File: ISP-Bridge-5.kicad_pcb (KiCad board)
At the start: 2 copper layers, 15.2 x 35.6 mm, 7 parts, among them IC1 ATMEGA328-P, J1 ATMEL_ISP_6PIN, SW1 SW_PUSH

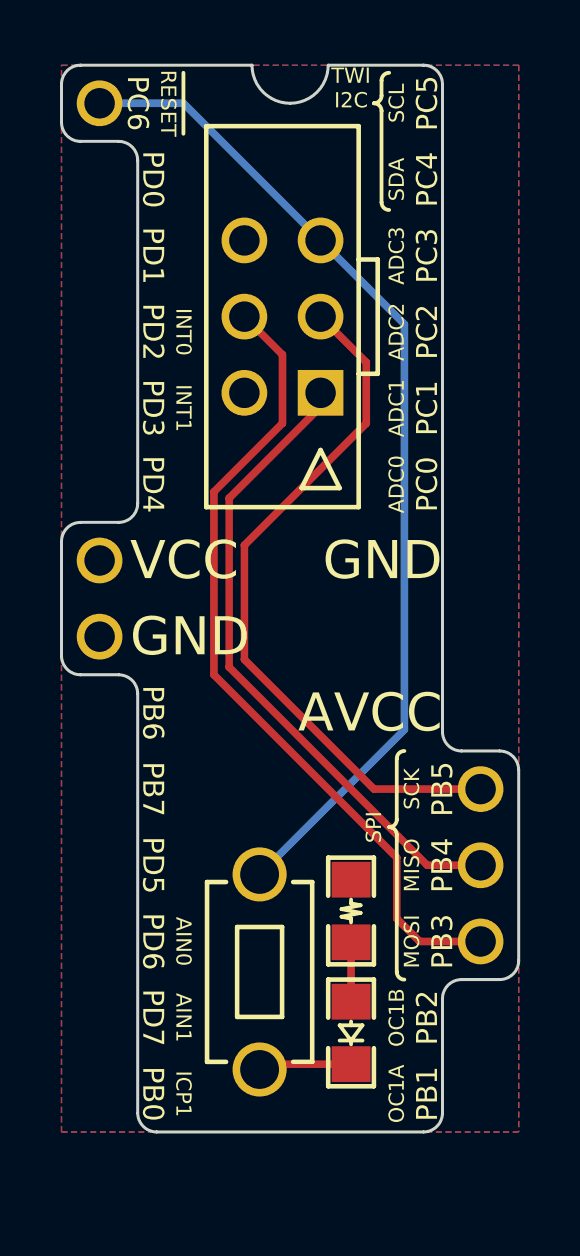
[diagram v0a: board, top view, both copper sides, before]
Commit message: Updated for KiCad 4.0.2, uses pretty libraries
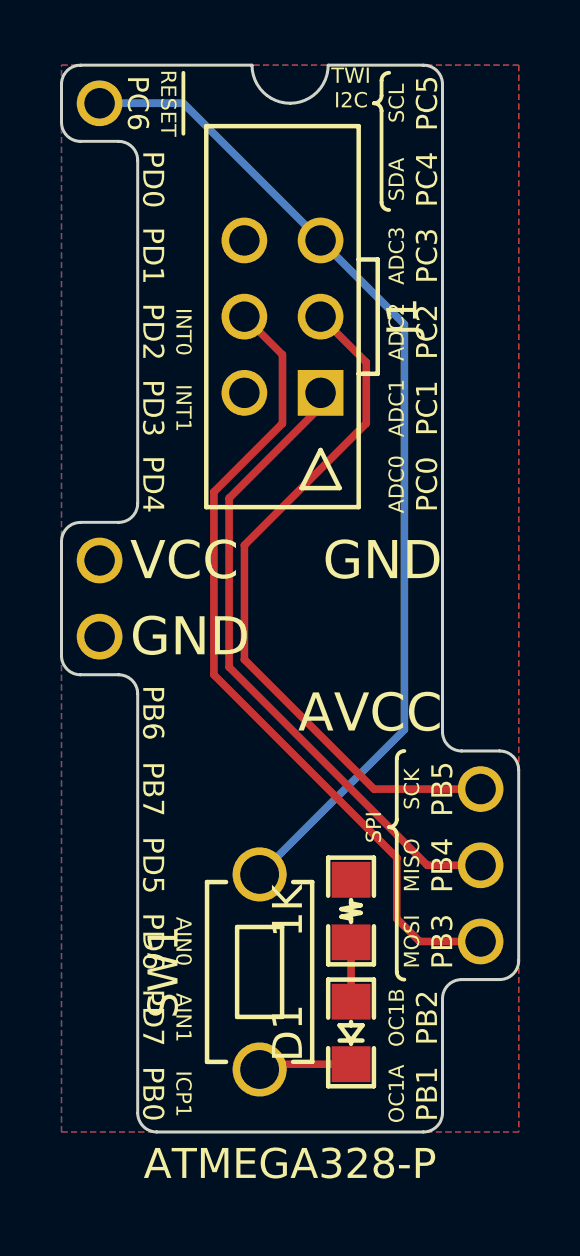
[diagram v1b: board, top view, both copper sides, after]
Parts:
- D1: footprint LED0805-sym -> Ossicone_Labs_Footprints:LED_0805_Symbol
- IC1: footprint ATmegax8 -> Ossicone_Labs_Footprints:Atmel_ATtiny-x8_ATmega-x8
- J1: footprint ATMEL_ISP_6PIN -> Ossicone_Labs_Footprints:Atmel_ISP_6PIN
- R1: footprint R0805-sym -> Ossicone_Labs_Footprints:R_0805_Symbol
- SW1: footprint MJTP1250 -> Ossicone_Labs_Footprints:SW_PUSH_MJTP1250
- turned D1 to 90 degrees
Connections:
- D1 pad 1: N-000004 -> GND
- D1 pad 2: GND -> Net-(D1-Pad2)
- R1 pad 1: N-000004 -> Net-(D1-Pad2)
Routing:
- net Net-(D1-Pad2): track 0.00 -> 1.98 mm
- net N-000004: track 1.98 -> 0.00 mm

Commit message: Rev 1.1 - changed rev number on board and 16 -> 32 segment on floodfills
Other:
- board text added: "v1.1"
- board text removed: "v1.0"
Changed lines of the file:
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@@
     (links 11)
     (no_connects 0)
-    (area 195.529999 107.899999 210.870001 143.560001)
+    (area 195.529999 105.701254 210.870001 145.608746)
     (thickness 1.6)
     (drawings 106)
@@
   (layers
     (0 F.Cu signal)
-    (31 B.Cu signal hide)
+    (31 B.Cu signal)
     (32 B.Adhes user hide)
     (33 F.Adhes user hide)
     (34 B.Paste user hide)
     (35 F.Paste user hide)
-    (36 B.SilkS user hide)
+    (36 B.SilkS user)
     (37 F.SilkS user)
-    (38 B.Mask user hide)
+    (38 B.Mask user)
     (39 F.Mask user)
     (40 Dwgs.User user hide)
@@
     (visible_elements 7FFCFF3F)
     (pcbplotparams
-      (layerselection 0x00030_80000001)
+      (layerselection 0x010f0_80000001)
       (usegerberextensions true)
       (excludeedgelayer true)
@@
       (net 7 "Net-(IC1-Pad17)"))
   )
-  (gr_text v1.0 (at 203.2 143.002) (layer B.SilkS)
+  (gr_text v1.1 (at 203.2 143.002) (layer B.SilkS)
     (effects (font (size 0.508 0.508) (thickness 0.127)) (justify mirror))
   )
@@
     (connect_pads (clearance 0.254))
     (min_thickness 0.1524)
-    (fill yes (arc_segments 16) (thermal_gap 0.254) (thermal_bridge_width 0.3048))
+    (fill yes (arc_segments 32) (thermal_gap 0.254) (thermal_bridge_width 0.3048))
     (polygon
       (pts
@@
     (connect_pads (clearance 0.1016))
     (min_thickness 0.1524)
-    (fill yes (arc_segments 16) (thermal_gap 0.254) (thermal_bridge_width 0.3048))
+    (fill yes (arc_segments 32) (thermal_gap 0.254) (thermal_bridge_width 0.3048))
     (polygon
       (pts

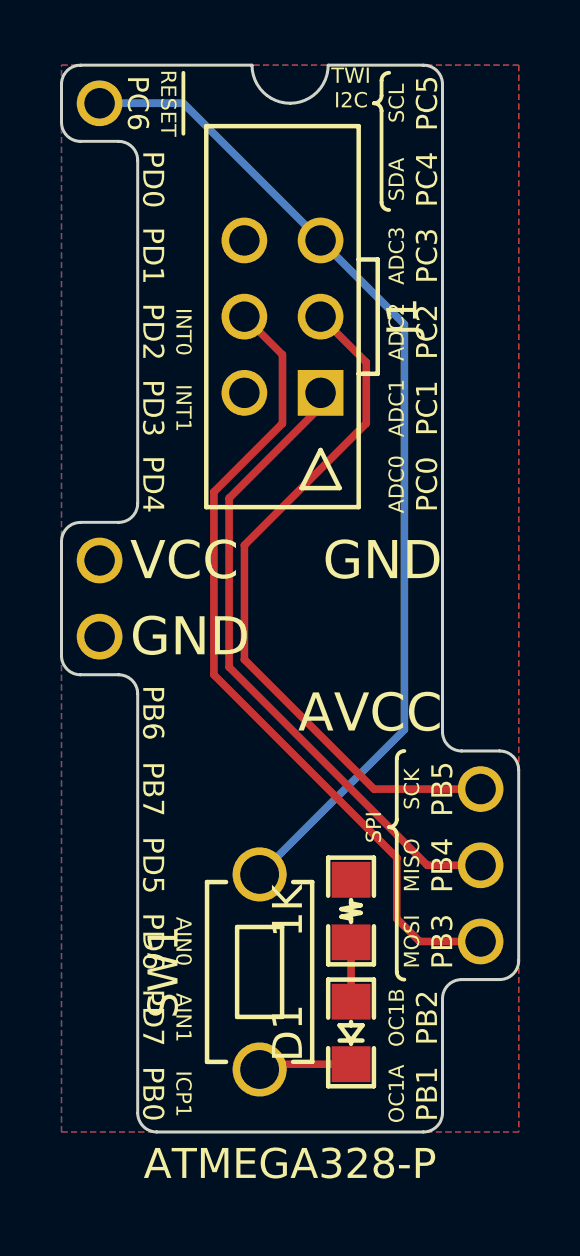
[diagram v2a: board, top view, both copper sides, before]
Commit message: Remove unused libs, update logo, increase to v1.1
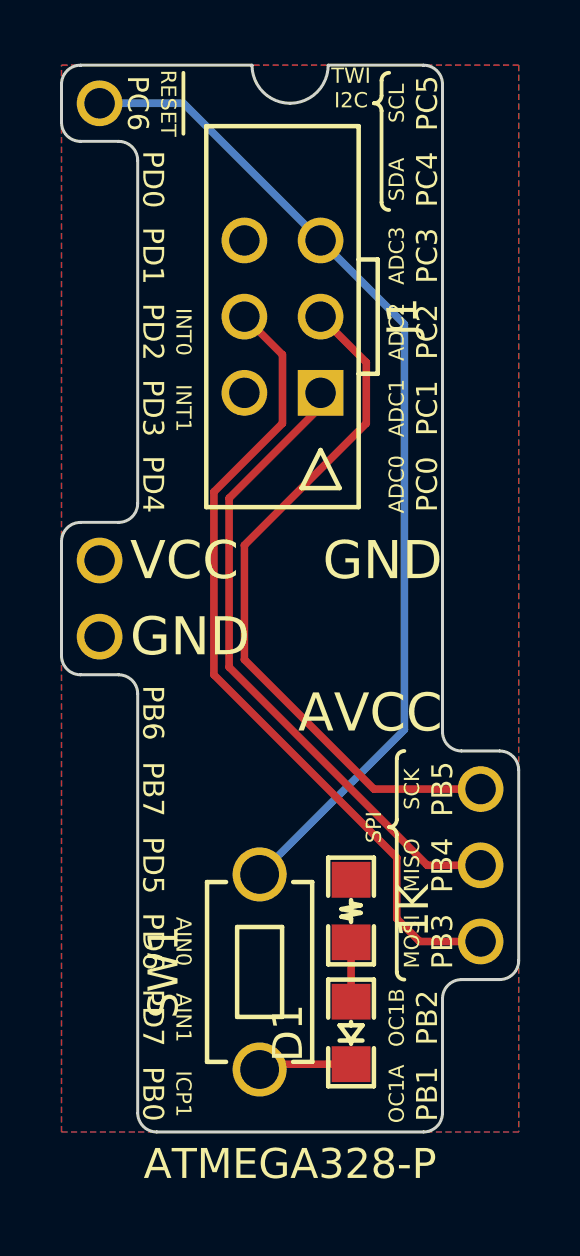
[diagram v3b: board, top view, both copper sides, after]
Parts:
- removed the VAL at (203.2, 123.7) (x2)
- added VAL: REF, Ossicone_Labs_Footprints:Ossicone_Labs_Logo_0.165prop_flipped, F.Cu at (203.2, 123.7)
- turned R1 to 270 degrees
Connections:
- R1 pad 1: Net-(D1-Pad2) -> VCC
- R1 pad 2: VCC -> Net-(D1-Pad2)
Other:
- board text added: "ISP BRIDGE 5"
- board text removed: "ISP BRIDGE"
